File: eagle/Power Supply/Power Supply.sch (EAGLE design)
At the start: 12 parts, among them IC1 ESP01, J1 FTDI, J2 DCJ0202, U1 LM7833

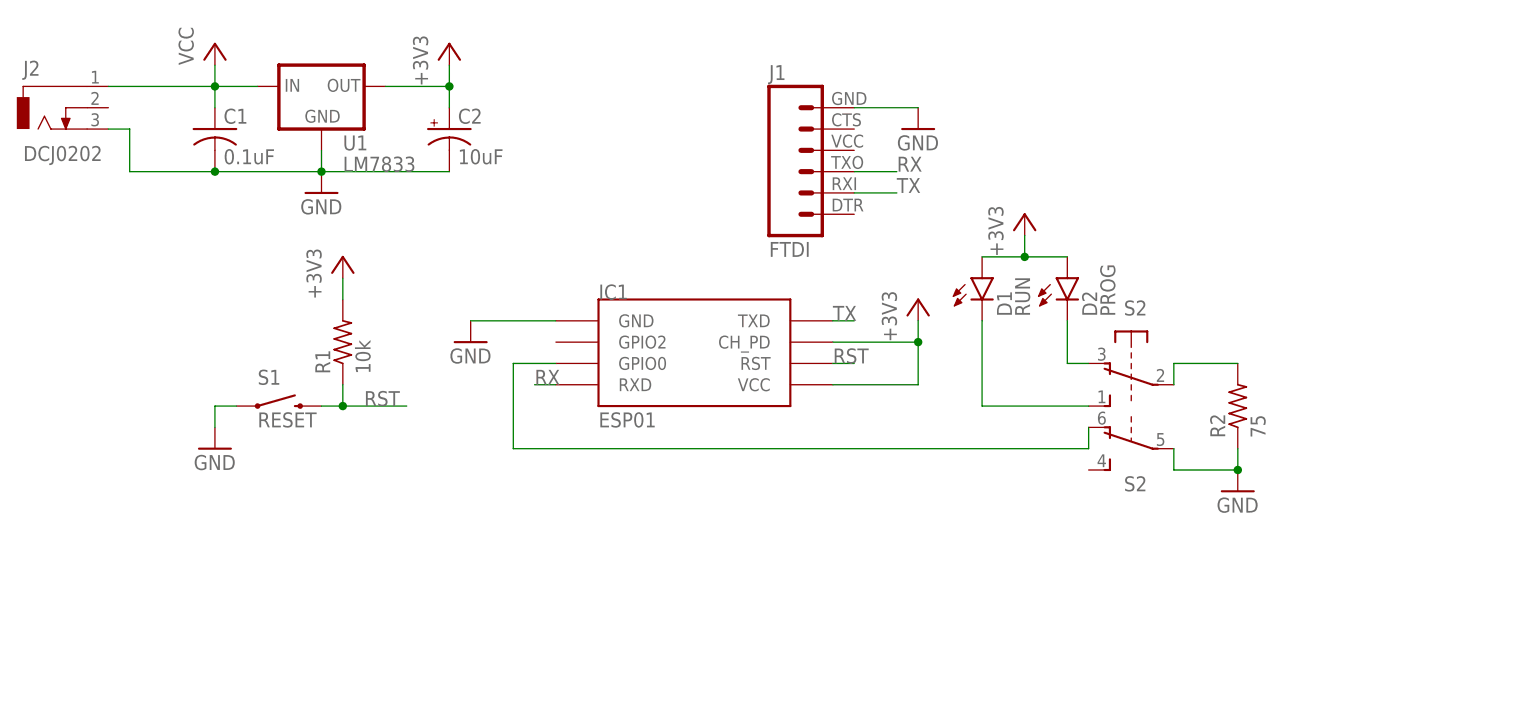
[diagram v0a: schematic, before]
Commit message: Power Supply regulator ref design
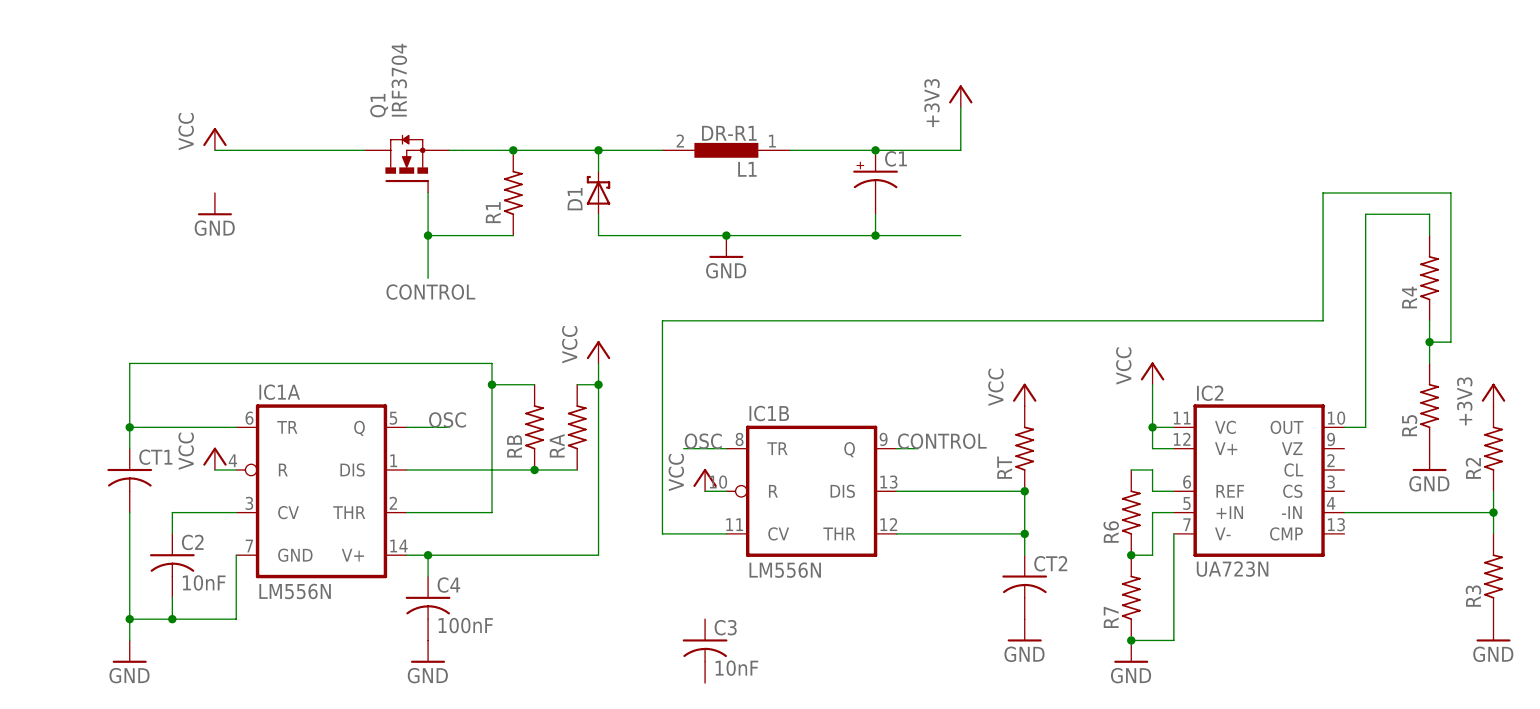
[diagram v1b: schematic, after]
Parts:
- removed D2: PROG, SparkFun-LED:LED3MM
- removed J1: FTDI, SparkFun-Connectors:FTDI_BASICPTH
- removed J2: DCJ0202, con-jack:DCJ0202
- removed S1: RESET, SparkFun-Electromechanical:SWITCH-MOMENTARY-2PTH
- removed S2: 9450-2, switch-misc:9450-2
- removed U1: LM7833, SparkFun-PowerIC:V_REG_78XX-TO-220
- added C3: 10nF, rcl:C-US050-025X075
- added C4: 100nF, rcl:C-US050-025X075
- added CT1, CT2: (no value), rcl:C-US050-025X075
- added IC2: UA723N, linear:UA723N
- added L1: DR-R1, inductors:DR-R1
- added Q1: IRF3704, transistor-power:IRF3704
- added R3, R4, R5, R6, R7, RA, RB, RT: (no value), rcl:R-US_0207/10
- C1: value 0.1uF -> (none); device rcl:C-US025-025X050 -> rcl:CPOL-USE7.5-18
- C2: value 10uF -> 10nF; device rcl:CPOL-USE2-4 -> rcl:C-US050-025X075
- D1: value RUN -> (none); device SparkFun-LED:LED3MM -> diode:SCHOTTKY-DIODEC4111-15
- IC1: value ESP01 -> LM556N; device esp8266modules:ESP01 -> linear:LM556N
- R1: value 10k -> (none)
- R2: value 75 -> (none)
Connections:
- removed net GPIO0: IC1.GPIO0, S22.O
- removed net RST: IC1.RST, R1.1, S1.2
- removed net RX: IC1.RXD, J1.3
- removed net TX: IC1.TXD, J1.2
- new net CONTROL: IC1B.Q, Q1.G, R1.1
- new net N$10: IC2.REF, R6.2
- new net N$11: IC2.+IN, R6.1, R7.2
- new net N$4: CT2.1, IC1B.DIS, IC1B.THR, RT.1
- new net N$5: IC2.-IN, R2.1, R3.2
- new net N$6: IC2.OUT, R4.2
- new net N$7: IC1B.CV, R4.1, R5.2
- new net N$8: C2.1, IC1A.CV
- new net OSC: IC1A.Q, IC1B.TR
- net +3V3: now also C1.+, L1.1, R2.2; no longer C2.+, D1.A, D2.A, IC1.CH_PD, IC1.VCC, R1.2, U1.OUT
- net GND: now also C1.-, C2.2, C4.2, CT1.2, CT2.2, D1.A, IC1A.GND, IC2.V-, R3.1, R5.1, R7.1; no longer C1.2, C2.-, IC1.GND, J1.6, J2.3, R2.1, S1.1, S22.P, U1.GND
- net N$1: now also D1.C, L1.2, Q1.S, R1.2; no longer D2.C, S21.O
- net N$2: now also CT1.1, IC1A.THR, IC1A.TR, RB.2; no longer R2.2, S21.P
- net N$3: now also IC1A.DIS, RA.1, RB.1; no longer D1.C, S21.S
- net VCC: now also C4.1, IC1A.R, IC1A.V+, IC1B.R, IC2.V+, IC2.VC, Q1.D, RA.2, RT.2; no longer C1.1, J2.1, U1.IN
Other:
- moved on the sheet: R1, R2
